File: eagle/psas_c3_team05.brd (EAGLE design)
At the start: 100 x 71.2 mm, 81 parts, among them IC1 CP2102, Q1 32 MHz, U1 MIC5219 3.3V, U2 MCP73871

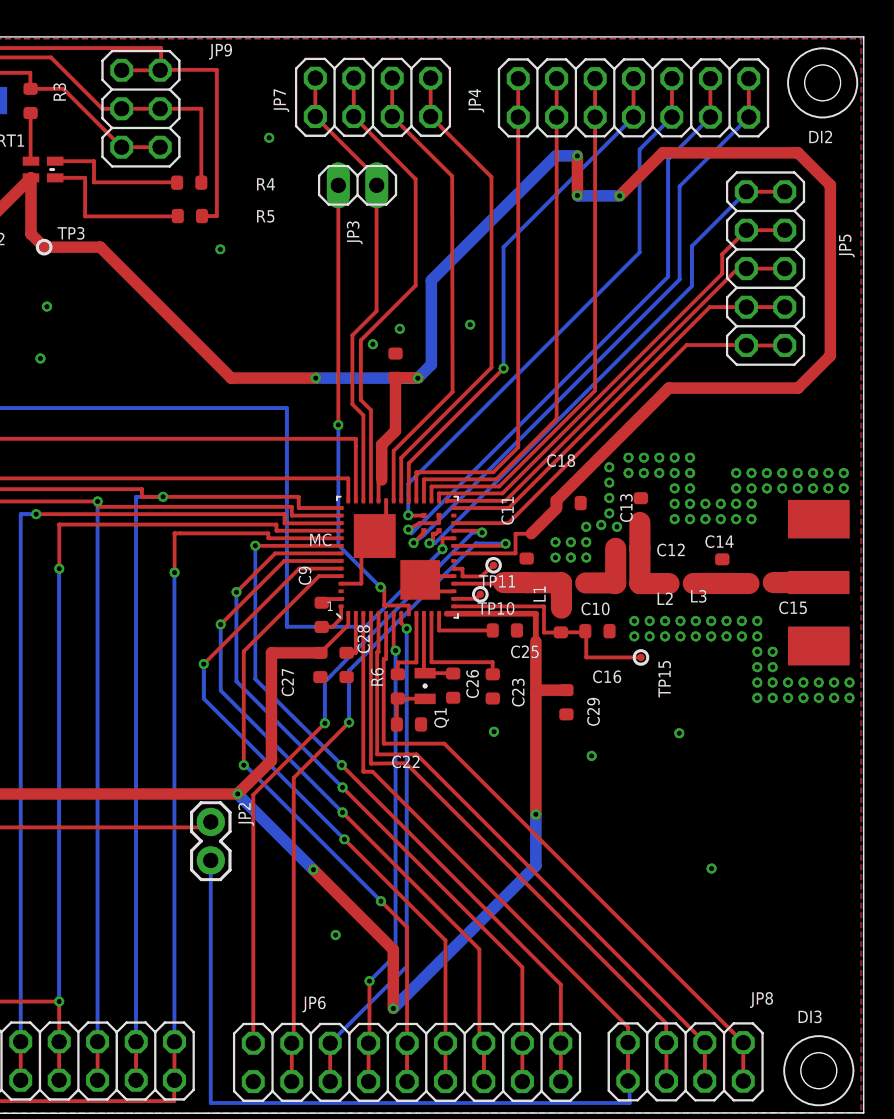
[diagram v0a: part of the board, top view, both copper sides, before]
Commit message: added labels for MCU ports on board layout, labeled some lines on PORTA of MCU that were missing labels
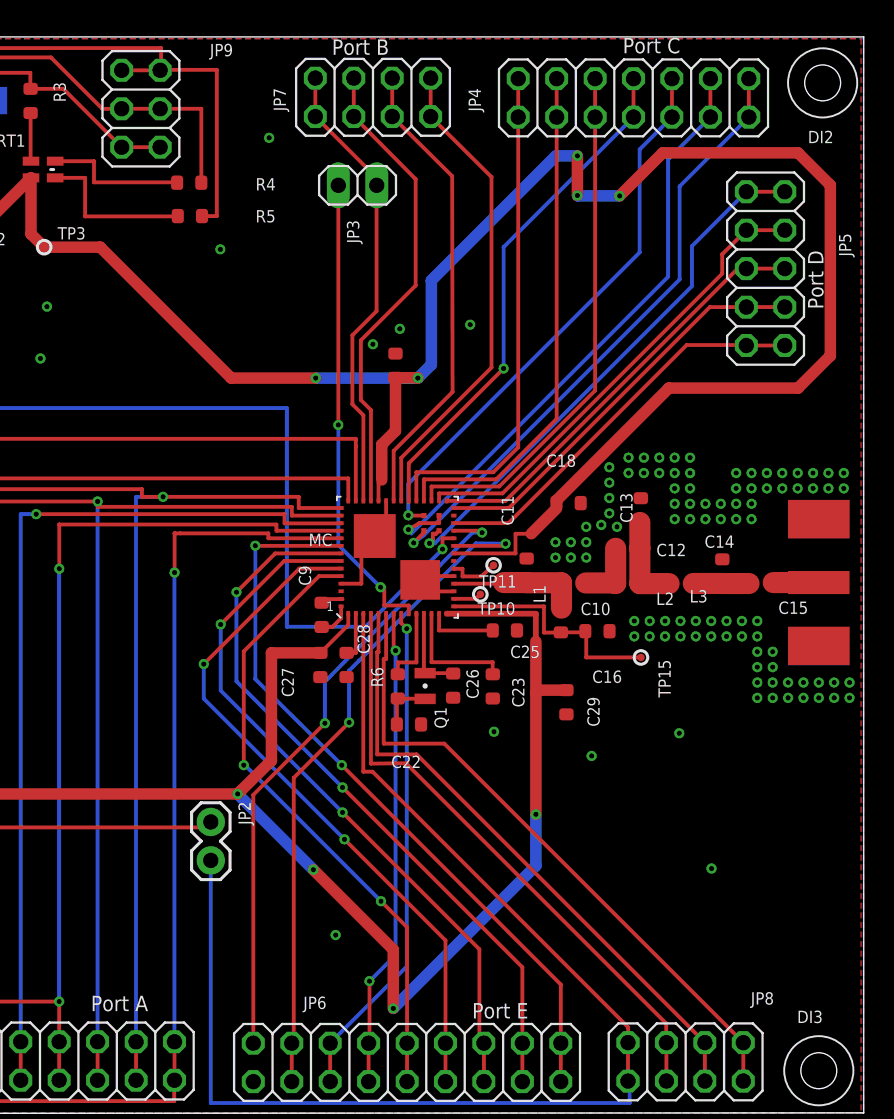
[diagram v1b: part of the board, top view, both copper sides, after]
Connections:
- net N$26 renamed PTA4
- net N$27 renamed PTA19/XTAL0
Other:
- board text added: "Port A"
- board text added: "Port B"
- board text added: "Port C"
- board text added: "Port D"
- board text added: "Port E"

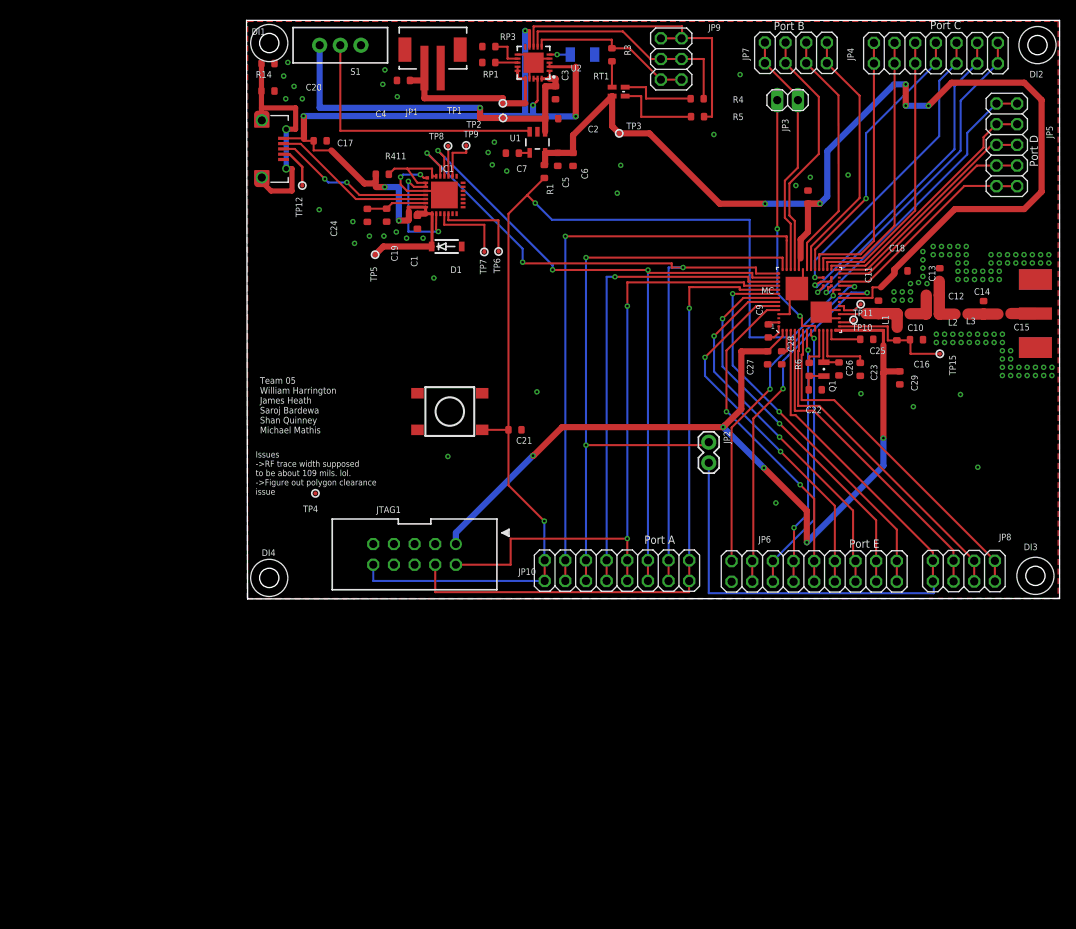
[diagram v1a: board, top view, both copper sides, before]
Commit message: General schematic clean a la Andrew -- Cap sizes, CP2102 test points and unused chips, killed VBUS diode, added power LED, Added TBG LED for KW0x that still needs to be connected, Misc OCD cleanup.
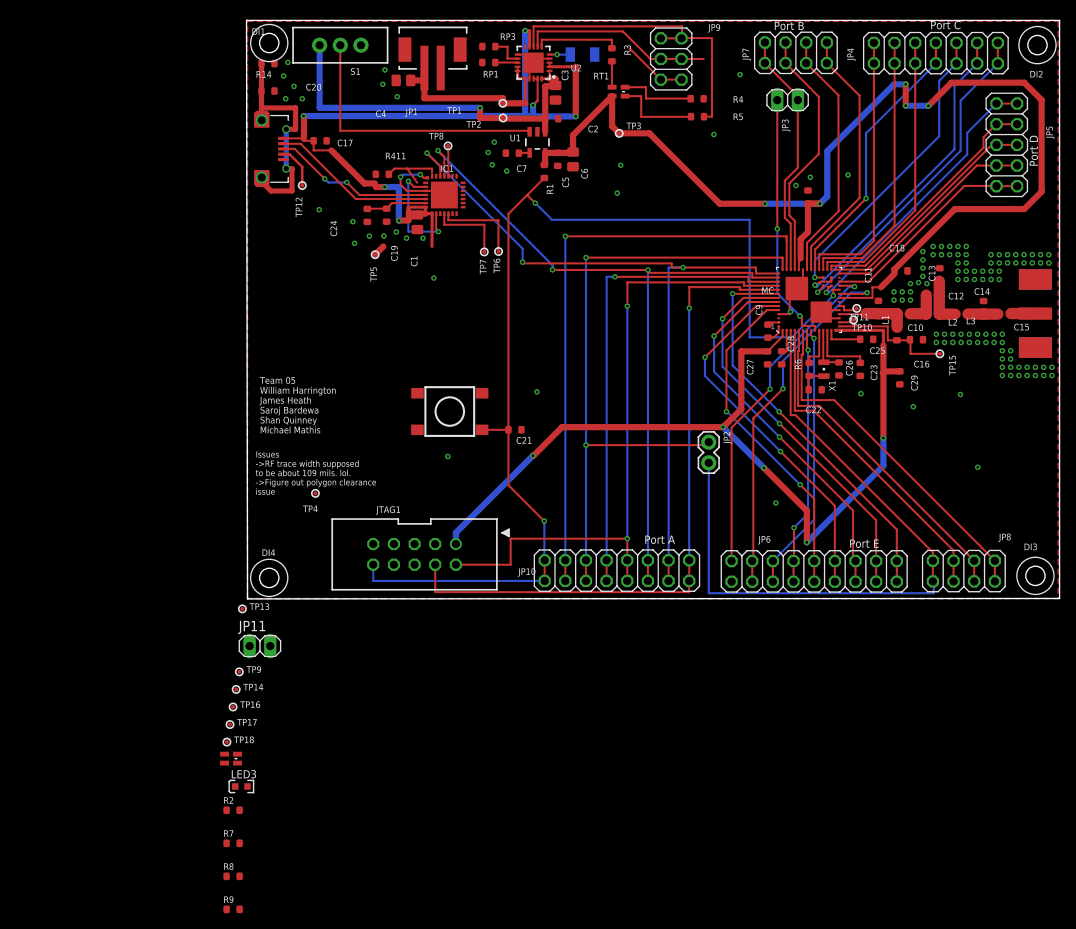
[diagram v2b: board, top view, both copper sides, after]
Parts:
- removed D1: (no value), Vibrogait_prototype:SOD-123
- added JP11: (no value), pinhead:1X02
- added LED2: APHFT1612PBASURKVGAC, Vibrogait_prototype:KINGBRITE_RGBLED_1.6X1.26
- added LED3: GRN, Vibrogait_prototype:LED-0603
- added R2, R7, R8, R9: 1k, rcl_custom:.0603-B-NOSILK
- added TP13, TP14, TP16, TP17, TP18: (no value), microbuilder:TESTPOINT_ROUND_0.5MM
- C1: value 10uF -> 4.7uF; device rcl_custom:.0603-B-NOSILK -> rcl_custom:.0805-B-NOSILK
- C3, C4: device rcl_custom:.0603-B-NOSILK -> rcl_custom:.0805-B-NOSILK
- C6: value 4.7uF -> 2.2uF; device rcl_custom:.0603-B-NOSILK -> rcl_custom:.0805-B-NOSILK
- LED1: value (none) -> APHFT1612PBASURKVGAC
- U1: value MIC5219 3.3V -> MIC5319 3.3V
- moved TP9 70.5 mm to (-0.89, -9.02), turned to 0 degrees
- moved TP11 0.70 mm to (75.1, 35.7)
- moved C9 0.05 mm to (64.1, 32.9)
- renumbered Q1 to X1
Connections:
- net N$34 renamed SHIELD
- new net N$26: IC1.28, TP9.P$1
- new net N$27: IC1.1, TP16.P$1
- new net N$28: IC1.27, TP17.P$1
- new net N$29: IC1.23, TP18.P$1
- new net N$31: LED3.K, R2.2
- net !PG: now also R4.1; no longer R3.1
- net 3.3V: now also LED3.A
- net GND: now also JP11.2, R2.1; no longer D1.ANODE
- net N$24: now also R411.1, TP13.P$1
- net N$25: now also IC1.2, TP14.P$1; no longer IC1.23, TP9.P$1
- net N$30: now also JP11.1; no longer IC1.1, IC1.2, IC1.27, IC1.28
- net STAT2: now also R3.1; no longer R4.1
- net VBUS: no longer D1.CATHODE, R411.1
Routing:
- net VBUS: track 108.6 -> 101.5 mm
- net N$25: track 5.55 -> 0.00 mm
- net STAT2: track 28.6 -> 23.7 mm
- net N$30: track 25.3 -> 22.8 mm
- net !PG: track 20.7 -> 18.5 mm
- net N$15: track 3.43 -> 2.74 mm
- net GND: vias 126 -> 127

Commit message: airwires for LED
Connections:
- new net N$32: LED2.1, R9.1
- new net N$33: LED2.4, R8.1
- new net N$34: LED2.3, R7.1
- net 3.3V: now also LED2.2
- net PTB1: now also R7.2
- net PTB17: now also R9.2
- net PTB2: now also R8.2
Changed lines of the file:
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@@
 <wire x1="64.190775" y1="32.131" x2="64.135" y2="32.093" width="0.254" layer="1"/>
 <contactref element="LED3" pad="A"/>
+<contactref element="LED2" pad="2"/>
 <wire x1="79.695140625" y1="40.302184375" x2="79.695140625" y2="39.946584375" width="0" layer="19" extent="1-1"/>
 <wire x1="72.434521875" y1="33.0034" x2="72.909521875" y2="36.9784" width="0" layer="19" extent="1-1"/>
 <wire x1="66.434521875" y1="33.0034" x2="65.934521875" y2="33.0034" width="0" layer="19" extent="1-1"/>
 <wire x1="65.459521875" y1="32.693521875" x2="65.934521875" y2="33.0034" width="0" layer="19" extent="1-1"/>
-<wire x1="0.115" y1="-23.114" x2="25.747984375" y2="6.7030625" width="0" layer="19" extent="1-1"/>
+<wire x1="-2.705" y1="-20.235" x2="25.747984375" y2="6.7030625" width="0" layer="19" extent="1-1"/>
+<wire x1="0.115" y1="-23.114" x2="-2.705" y2="-20.235" width="0" layer="19" extent="1-1"/>
 </signal>
 <signal name="VBUS">
@@
 <wire x1="70.385940625" y1="54.67858125" x2="70.385940625" y2="61.709303125" width="0.254" layer="1"/>
 <wire x1="70.385940625" y1="61.709303125" x2="66.29908125" y2="65.8469625" width="0.254" layer="1"/>
+<contactref element="R7" pad="2"/>
+<wire x1="-0.851" y1="-30.099" x2="67.434521875" y2="40.4534" width="0" layer="19" extent="1-1"/>
 </signal>
 <signal name="PTB2">
@@
 <wire x1="72.82688125" y1="47.64531875" x2="72.80148125" y2="61.9099625" width="0.254" layer="1"/>
 <wire x1="72.80148125" y1="61.9099625" x2="68.83908125" y2="65.8469625" width="0.254" layer="1"/>
+<contactref element="R8" pad="2"/>
+<wire x1="-0.851" y1="-34.163" x2="68.934521875" y2="40.4534" width="0" layer="19" extent="1-1"/>
 </signal>
 <signal name="PTB17">
@@
 <wire x1="75.3999" y1="49.260759375" x2="75.3999" y2="61.85154375" width="0.254" layer="1"/>
 <wire x1="75.3999" y1="61.85154375" x2="71.37908125" y2="65.8469625" width="0.254" layer="1"/>
+<contactref element="R9" pad="2"/>
+<wire x1="-0.851" y1="-38.227" x2="69.434521875" y2="40.4534" width="0" layer="19" extent="1-1"/>
 </signal>
 <signal name="DIO5/CLKOUT">
@@
 <wire x1="-1.385" y1="-23.114" x2="-0.851" y2="-26.035" width="0" layer="19" extent="1-1"/>
 </signal>
+<signal name="N$32">
+<contactref element="LED2" pad="1"/>
+<contactref element="R9" pad="1"/>
+<wire x1="-1.105" y1="-20.235" x2="-2.451" y2="-38.227" width="0" layer="19" extent="1-1"/>
+</signal>
+<signal name="N$33">
+<contactref element="LED2" pad="4"/>
+<contactref element="R8" pad="1"/>
+<wire x1="-1.105" y1="-19.135" x2="-2.451" y2="-34.163" width="0" layer="19" extent="1-1"/>
+</signal>
+<signal name="N$34">
+<contactref element="LED2" pad="3"/>
+<contactref element="R7" pad="1"/>
+<wire x1="-2.705" y1="-19.135" x2="-2.451" y2="-30.099" width="0" layer="19" extent="1-1"/>
+</signal>
 </signals>

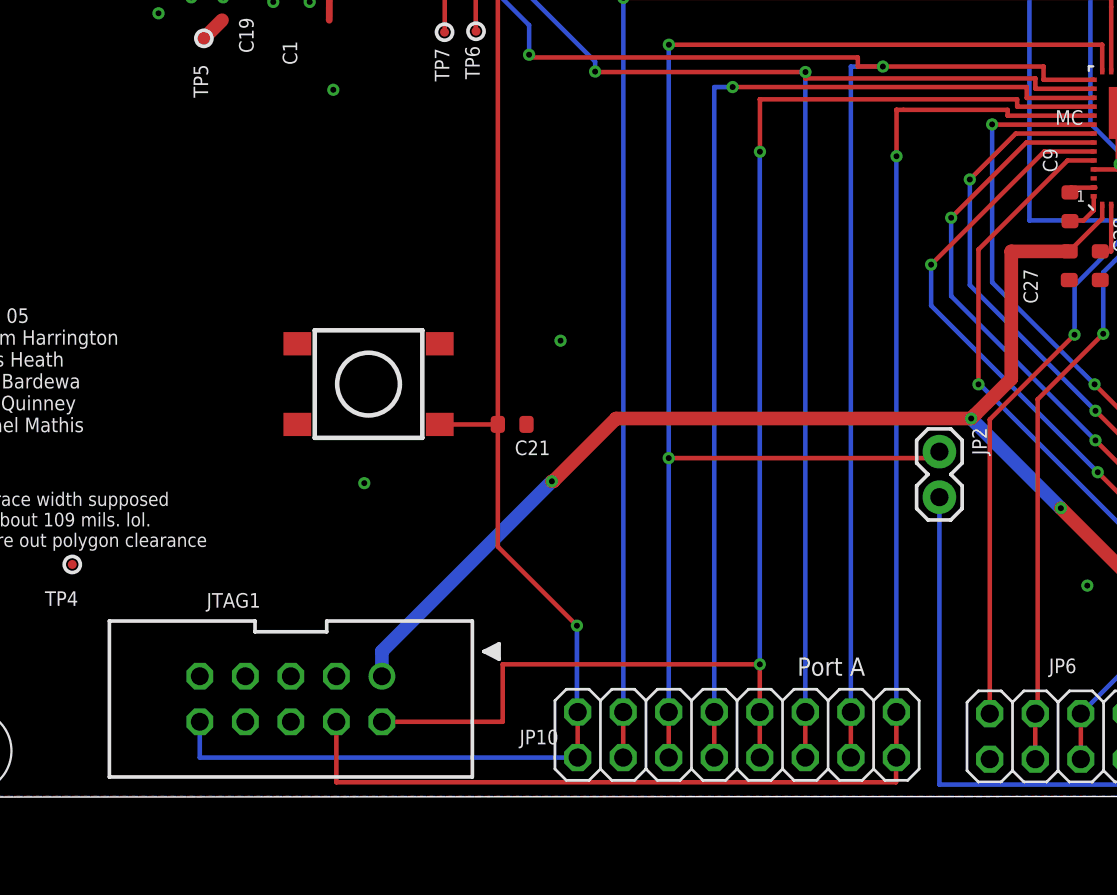
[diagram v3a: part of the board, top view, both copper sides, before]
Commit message: Swtiched JTAG/SWD connector and added part values for missing values.
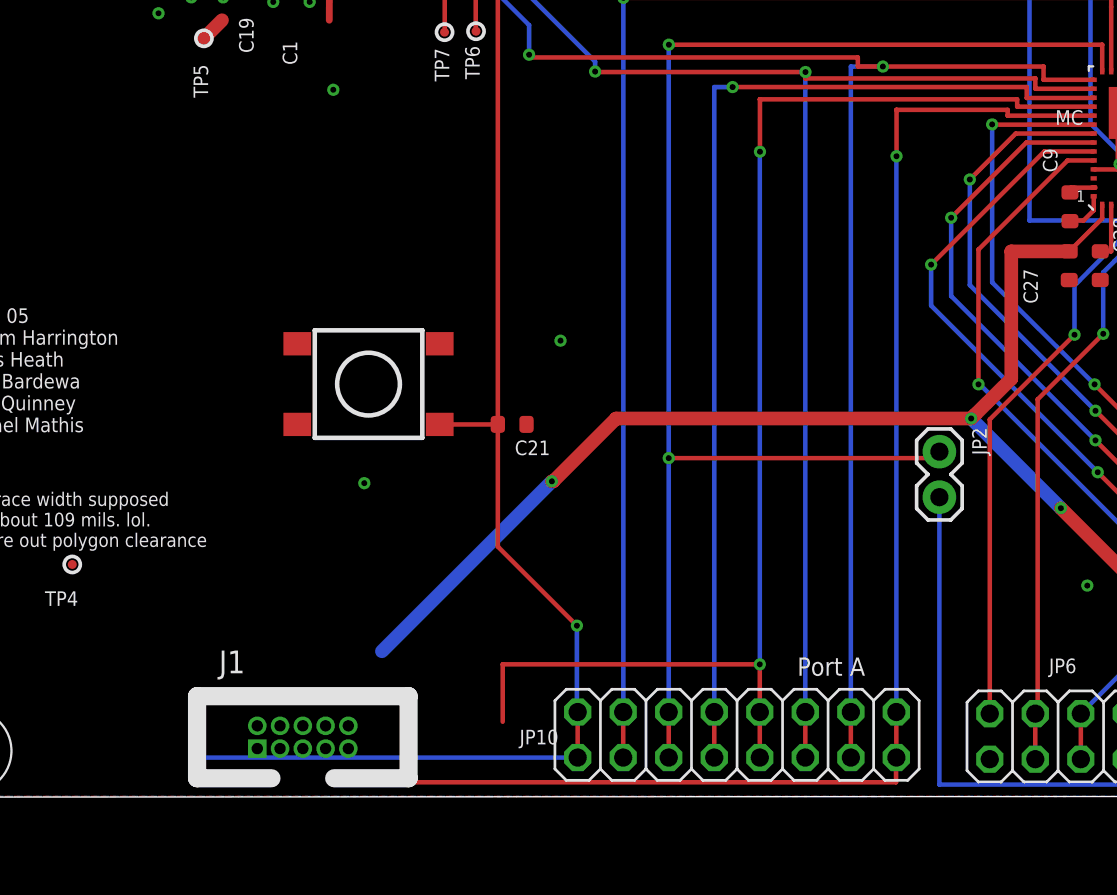
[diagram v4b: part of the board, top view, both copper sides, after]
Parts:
- removed JTAG1: (no value), microbuilder:CORTEXM3_SWD10_MOLEX
- added J1: 3220-10-0100-00, apdm-ic-v2:PINHEADER-2X5-0.05+POL+SILK
- S1: value (none) -> EG1218
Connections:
- net N$24 renamed CP2102_VDD
- net 3.3V: now also J1.1; no longer JTAG1.1
- net GND: now also J1.3, J1.5, J1.9; no longer JTAG1.3, JTAG1.5, JTAG1.9
- net PTA0: now also J1.4; no longer JTAG1.4
- net PTA20/!RESET: now also J1.10; no longer JTAG1.10
- net PTA3: now also J1.2; no longer JTAG1.2
- net PTE0: now also JP6.1
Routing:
- net PTA3: track 80.1 -> 73.3 mm
- net PTA0: track 83.5 -> 80.1 mm
- net PTA20/!RESET: track 136.6 -> 134.6 mm
- net 3.3V: track 259.6 -> 258.2 mm
